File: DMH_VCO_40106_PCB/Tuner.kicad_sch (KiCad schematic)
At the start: 20 parts, among them J11 AVR-ISP-6, SW3 SW_SPDT, U5 ATtiny84A-P, U6 SM420561N

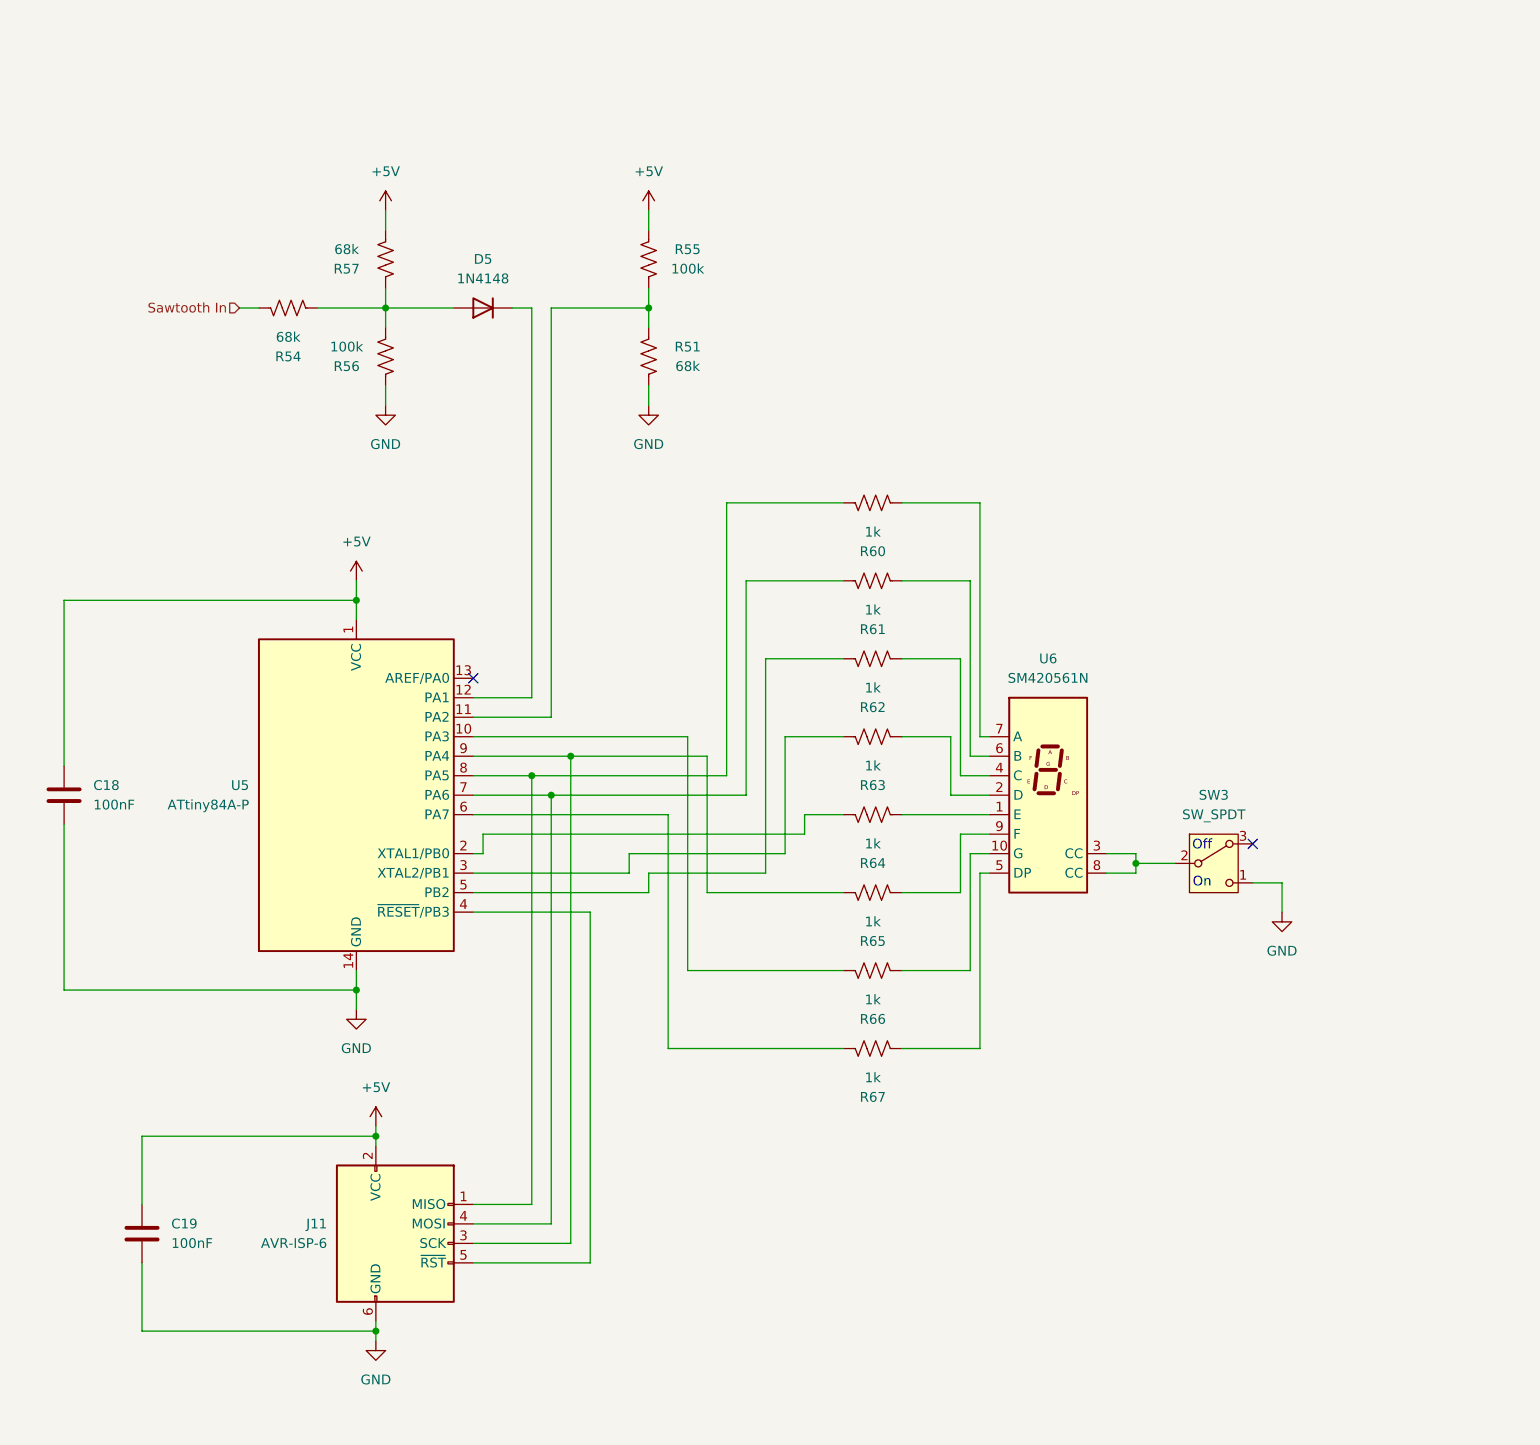
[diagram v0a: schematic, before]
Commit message: Updated Tuner
- Changed uC to ATtiny4313
- Added LEDs
- Created "function" field and updated all jacks, switches and pots
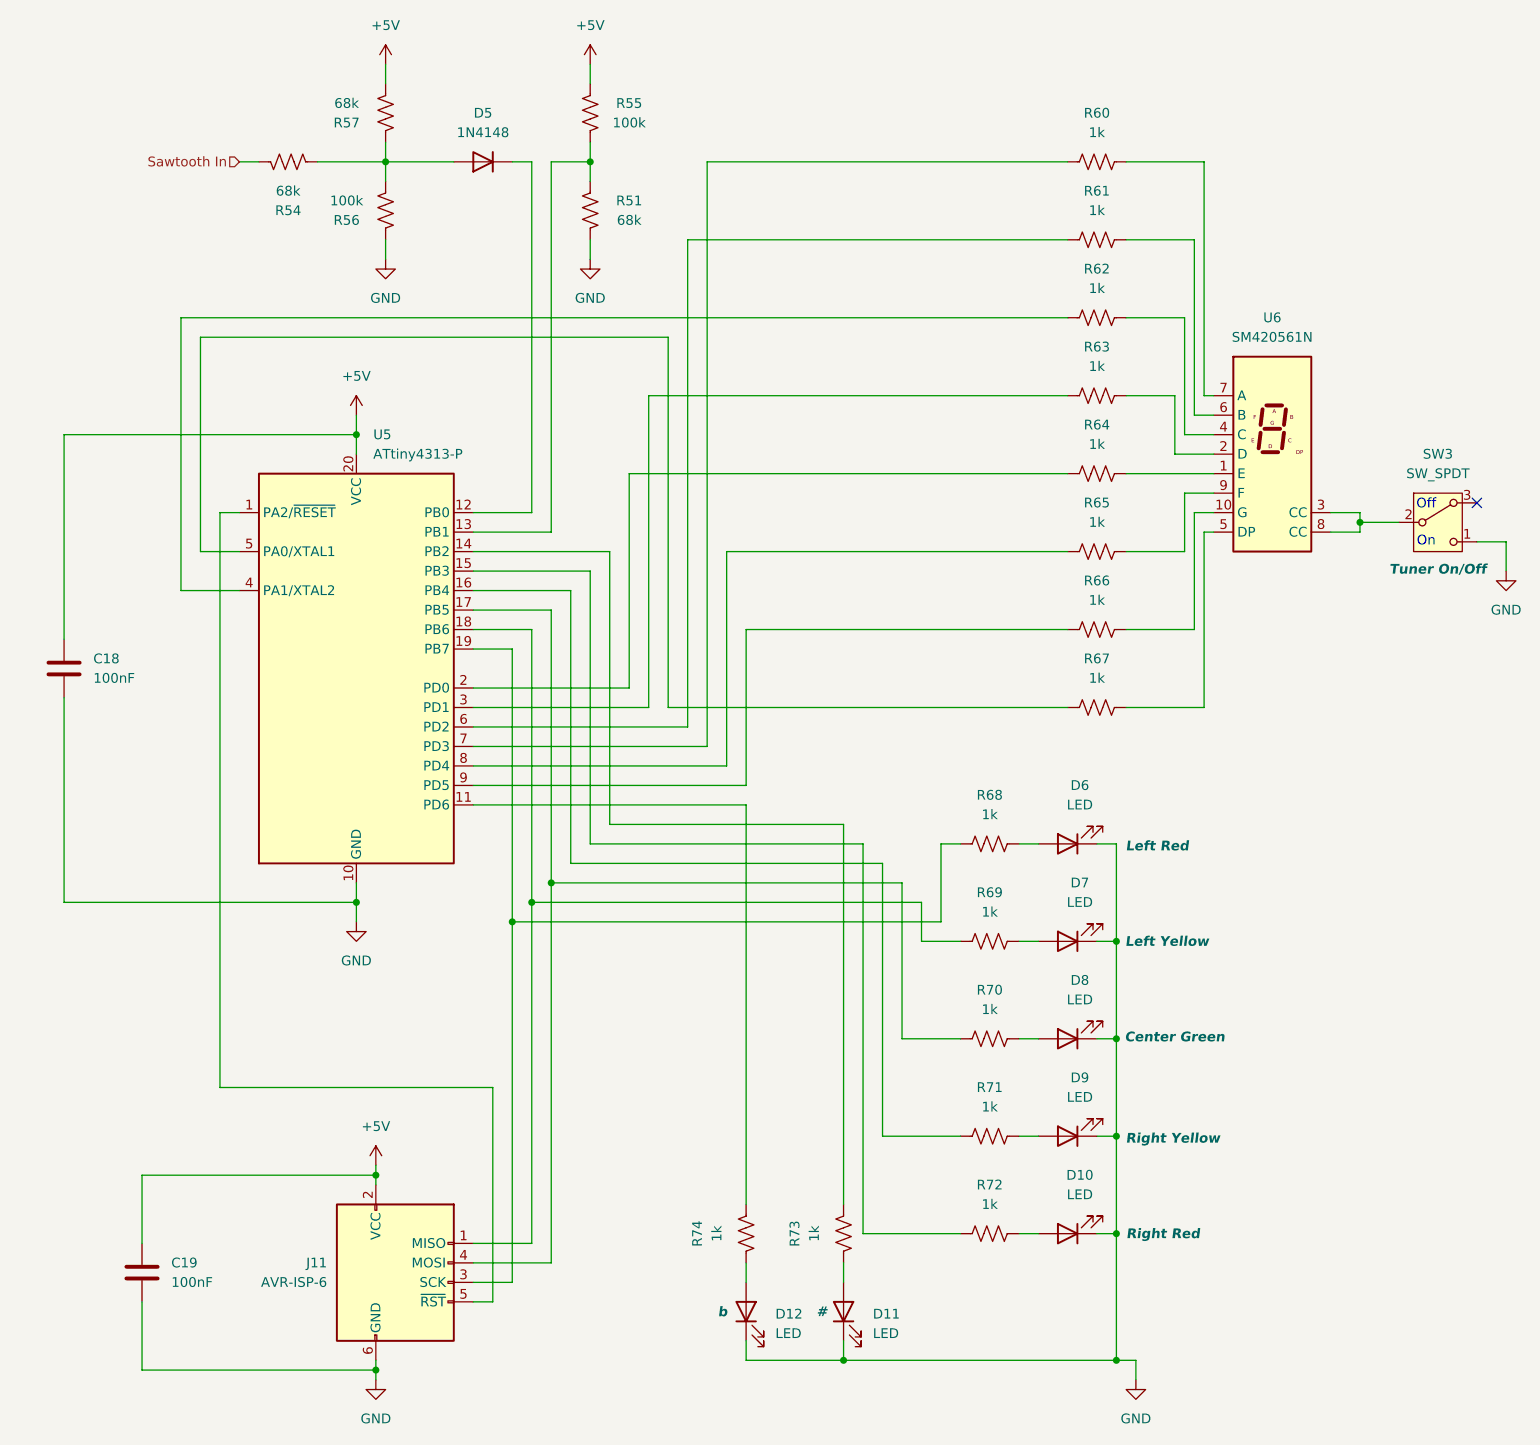
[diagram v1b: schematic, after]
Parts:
- added D10, D11, D12, D6, D7, D8, D9: LED, symbol Device:LED
- added R68, R69, R70, R71, R72, R73, R74: 1k, Resistor_THT:R_Axial_DIN0204_L3.6mm_D1.6mm_P5.08mm_Horizontal, symbol Device:R_US
- SW3: Function (none) -> Tuner On/Off
- U5: value ATtiny84A-P -> ATtiny4313-P; footprint Package_DIP:DIP-14_W7.62mm -> Package_DIP:DIP-20_W7.62mm; symbol MCU_Microchip_ATtiny:ATtiny84A-P -> MCU_Microchip_ATtiny:ATtiny4313-P
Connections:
- net +5V: now also U5.20 (VCC); no longer U5.1 (VCC)
- net GND: now also U5.10 (GND), D10.1 (K), D11.1 (K), D12.1 (K), D6.1 (K), D7.1 (K), D8.1 (K), D9.1 (K); no longer U5.14 (GND)
- net at R66.1: now also U5.9 (PD5); no longer U5.10 (PA3)
- net at R51.2, R55.1: now also U5.13 (PB1); no longer U5.11 (PA2)
- net at J11.5 (~{RST}): now also U5.1 (PA2/~{RESET}); no longer U5.4 (~{RESET}/PB3)
- net at R62.1: now also U5.4 (PA1/XTAL2); no longer U5.5 (PB2)
- net at R67.1: now also U5.5 (PA0/XTAL1); no longer U5.6 (PA7)
- new net: J11.3 (SCK), R68.1, U5.19 (PB7)
- new net: D6.2 (A), R68.2
- new net: R60.1, U5.7 (PD3)
- new net: D12.2 (A), R74.2
- new net: R71.1, U5.16 (PB4)
- new net: D9.2 (A), R71.2
- new net: J11.4 (MOSI), R70.1, U5.17 (PB5)
- new net: D8.2 (A), R70.2
- new net: R74.1, U5.11 (PD6)
- new net: R73.1, U5.14 (PB2)
- new net: R72.1, U5.15 (PB3)
- new net: J11.1 (MISO), R69.1, U5.18 (PB6)
- new net: R61.1, U5.6 (PD2)
- new net: R65.1, U5.8 (PD4)
- new net: D10.2 (A), R72.2
- new net: D11.2 (A), R73.2
- new net: D7.2 (A), R69.2
- no-connect marks 2 -> 1
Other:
- moved on the sheet: C18, C19, D5, J11, R51, R54, R55, R56, R57, R60, R61, R62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

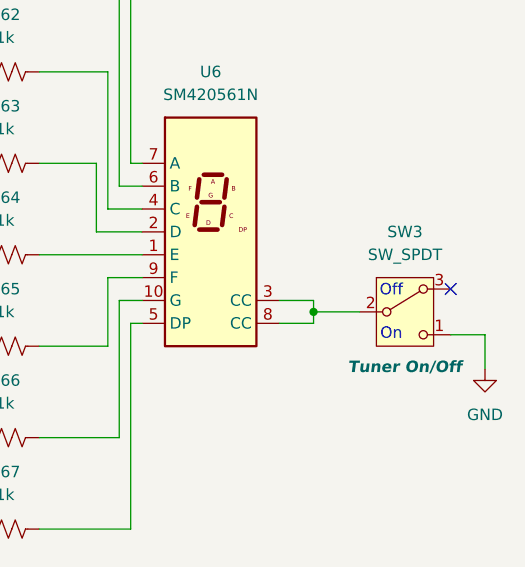
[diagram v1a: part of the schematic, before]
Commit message: Prepared Inputs/Outputs sheet to split in 2 PCBs
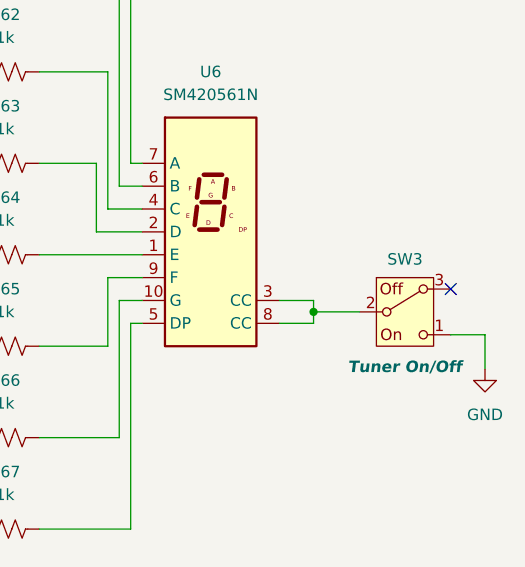
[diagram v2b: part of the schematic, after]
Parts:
- SW3: value SW_SPDT -> SW_SPDT_321_OnOff; symbol Switch:SW_SPDT_321 -> SynthStuff:SW_SPDT_321_OnOff
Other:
- note removed: "Off"
- note removed: "On"
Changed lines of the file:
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@@
-		)
-	)
-	(text "Off"
-		(exclude_from_sim no)
-		(at 202.946 76.454 0)
-		(effects
-			(font
-				(size 1.27 1.27)
-			)
-		)
-	)
-	(text "On"
-		(exclude_from_sim no)
-		(at 202.946 81.28 0)
-		(effects
-			(font
-				(size 1.27 1.27)
-			)
 		)
 	)
@@
 	)
 	(symbol
-		(lib_id "Switch:SW_SPDT_321")
+		(lib_id "SynthStuff:SW_SPDT_321_OnOff")
 		(at 204.47 78.74 0)
 		(unit 1)
@@
 		(dnp no)
 		(property "Reference" "SW3"
-			(at 204.47 69.85 0)
-			(effects
-				(font
-					(size 1.27 1.27)
-				)
-			)
-		)
-		(property "Value" "SW_SPDT"
-			(at 204.47 72.39 0)
-			(effects
-				(font
-					(size 1.27 1.27)
-				)
-			)
-		)
+			(at 204.47 72.898 0)
+			(effects
+				(font
+					(size 1.27 1.27)
+				)
+			)
+		)
+		(property "Value" "SW_SPDT_321_OnOff"
+			(at 204.47 83.82 0)
+			(effects
+				(font
+					(size 1.27 1.27)
+				)
+				(hide yes)
+			)
+		)

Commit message: Started positioning components on PCB
Moving some input resistores from main PCB to Jacks PCB
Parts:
- D10, D11, D12, D6, D7, D8, D9: footprint (none) -> LED_THT:LED_D3.0mm
- R51, R54, R55, R56, R57, R60, R61, R62, R63, R64, R65, R66, R67, R68, R69, R70, R71, R72, R73, R74: footprint Resistor_THT:R_Axial_DIN0204_L3.6mm_D1.6mm_P5.08mm_Horizontal -> Resistor_THT:R_Axial_DIN0207_L6.3mm_D2.5mm_P7.62mm_Horizontal
- SW3: footprint (none) -> SynthStuff:Toggle_Switch_THT
- U5: footprint Package_DIP:DIP-20_W7.62mm -> Package_DIP:DIP-20_W7.62mm_Socket
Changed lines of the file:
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@@
 			)
 		)
-		(property "Footprint" "Resistor_THT:R_Axial_DIN0204_L3.6mm_D1.6mm_P5.08mm_Horizontal"
+		(property "Footprint" "Resistor_THT:R_Axial_DIN0207_L6.3mm_D2.5mm_P7.62mm_Horizontal"
 			(at 146.304 119.634 90)
 			(effects
@@
 			)
 		)
-		(property "Footprint" "Resistor_THT:R_Axial_DIN0204_L3.6mm_D1.6mm_P5.08mm_Horizontal"
+		(property "Footprint" "Resistor_THT:R_Axial_DIN0207_L6.3mm_D2.5mm_P7.62mm_Horizontal"
 			(at 160.274 91.694 90)
 			(effects
@@
 			)
 		)
-		(property "Footprint" "Resistor_THT:R_Axial_DIN0204_L3.6mm_D1.6mm_P5.08mm_Horizontal"
+		(property "Footprint" "Resistor_THT:R_Axial_DIN0207_L6.3mm_D2.5mm_P7.62mm_Horizontal"
 			(at 160.274 30.734 90)
 			(effects
@@
 			)
 		)
-		(property "Footprint" ""
+		(property "Footprint" "LED_THT:LED_D3.0mm"
 			(at 114.3 181.61 0)
 			(effects
@@
 			)
 		)
-		(property "Footprint" "Resistor_THT:R_Axial_DIN0204_L3.6mm_D1.6mm_P5.08mm_Horizontal"
+		(property "Footprint" "Resistor_THT:R_Axial_DIN0207_L6.3mm_D2.5mm_P7.62mm_Horizontal"
 			(at 146.304 157.734 90)
 			(effects
@@
 			)
 		)
-		(property "Footprint" "Resistor_THT:R_Axial_DIN0204_L3.6mm_D1.6mm_P5.08mm_Horizontal"
+		(property "Footprint" "Resistor_THT:R_Axial_DIN0207_L6.3mm_D2.5mm_P7.62mm_Horizontal"
 			(at 146.304 145.034 90)
 			(effects
@@
 			)
 		)
-		(property "Footprint" "Resistor_THT:R_Axial_DIN0204_L3.6mm_D1.6mm_P5.08mm_Horizontal"
+		(property "Footprint" "Resistor_THT:R_Axial_DIN0207_L6.3mm_D2.5mm_P7.62mm_Horizontal"
 			(at 66.294 25.654 90)
 			(effects
@@
 			)
 		)
-		(property "Footprint" "Package_DIP:DIP-20_W7.62mm"
+		(property "Footprint" "Package_DIP:DIP-20_W7.62mm_Socket"
 			(at 63.5 97.79 0)
 			(effects
@@
 			)
 		)
-		(property "Footprint" "Resistor_THT:R_Axial_DIN0204_L3.6mm_D1.6mm_P5.08mm_Horizontal"
+		(property "Footprint" "Resistor_THT:R_Axial_DIN0207_L6.3mm_D2.5mm_P7.62mm_Horizontal"
 			(at 160.274 40.894 90)
 			(effects
@@
 			)
 		)
-		(property "Footprint" "Resistor_THT:R_Axial_DIN0204_L3.6mm_D1.6mm_P5.08mm_Horizontal"
+		(property "Footprint" "Resistor_THT:R_Axial_DIN0207_L6.3mm_D2.5mm_P7.62mm_Horizontal"
 			(at 160.274 61.214 90)
 			(effects
@@
 			)
 		)
-		(property "Footprint" "Resistor_THT:R_Axial_DIN0204_L3.6mm_D1.6mm_P5.08mm_Horizontal"
+		(property "Footprint" "Resistor_THT:R_Axial_DIN0207_L6.3mm_D2.5mm_P7.62mm_Horizontal"
 			(at 94.996 37.846 90)
 			(effects
@@
 			)
 		)
-		(property "Footprint" ""
+		(property "Footprint" "LED_THT:LED_D3.0mm"
 			(at 156.21 171.45 0)
 			(effects
@@
 			)
 		)
-		(property "Footprint" "Resistor_THT:R_Axial_DIN0204_L3.6mm_D1.6mm_P5.08mm_Horizontal"
+		(property "Footprint" "Resistor_THT:R_Axial_DIN0207_L6.3mm_D2.5mm_P7.62mm_Horizontal"
 			(at 160.274 101.854 90)
 			(effects
@@
 			)
 		)
-		(property "Footprint" "Resistor_THT:R_Axial_DIN0204_L3.6mm_D1.6mm_P5.08mm_Horizontal"
+		(property "Footprint" "Resistor_THT:R_Axial_DIN0207_L6.3mm_D2.5mm_P7.62mm_Horizontal"
 			(at 160.274 81.534 90)
 			(effects
@@
 			)
 		)
-		(property "Footprint" "Resistor_THT:R_Axial_DIN0204_L3.6mm_D1.6mm_P5.08mm_Horizontal"
+		(property "Footprint" "Resistor_THT:R_Axial_DIN0207_L6.3mm_D2.5mm_P7.62mm_Horizontal"
 			(at 66.294 38.354 90)
 			(effects
@@
 			)
 		)
-		(property "Footprint" ""
+		(property "Footprint" "LED_THT:LED_D3.0mm"
 			(at 127 181.61 0)
 			(effects
@@
 			)
 		)
-		(property "Footprint" ""
+		(property "Footprint" "LED_THT:LED_D3.0mm"
 			(at 156.21 120.65 0)
 			(effects
@@
 			)
 		)
-		(property "Footprint" "Resistor_THT:R_Axial_DIN0204_L3.6mm_D1.6mm_P5.08mm_Horizontal"
+		(property "Footprint" "Resistor_THT:R_Axial_DIN0207_L6.3mm_D2.5mm_P7.62mm_Horizontal"
 			(at 146.304 132.334 90)
 			(effects
@@
 			)
 		)
-		(property "Footprint" "Resistor_THT:R_Axial_DIN0204_L3.6mm_D1.6mm_P5.08mm_Horizontal"
+		(property "Footprint" "Resistor_THT:R_Axial_DIN0207_L6.3mm_D2.5mm_P7.62mm_Horizontal"
 			(at 113.284 171.704 90)
 			(effects
@@
 			)
 		)
-		(property "Footprint" ""
+		(property "Footprint" "SynthStuff:Toggle_Switch_THT"
 			(at 204.47 88.9 0)
 			(effects
@@
 			)
 		)
-		(property "Footprint" "Resistor_THT:R_Axial_DIN0204_L3.6mm_D1.6mm_P5.08mm_Horizontal"
+		(property "Footprint" "Resistor_THT:R_Axial_DIN0207_L6.3mm_D2.5mm_P7.62mm_Horizontal"
 			(at 146.304 170.434 90)
 			(effects
@@
 			)
 		)
-		(property "Footprint" "Resistor_THT:R_Axial_DIN0204_L3.6mm_D1.6mm_P5.08mm_Horizontal"
+		(property "Footprint" "Resistor_THT:R_Axial_DIN0207_L6.3mm_D2.5mm_P7.62mm_Horizontal"
 			(at 160.274 51.054 90)
 			(effects
@@
 			)
 		)
-		(property "Footprint" "Resistor_THT:R_Axial_DIN0204_L3.6mm_D1.6mm_P5.08mm_Horizontal"
+		(property "Footprint" "Resistor_THT:R_Axial_DIN0207_L6.3mm_D2.5mm_P7.62mm_Horizontal"
 			(at 54.864 32.766 90)
 			(effects
@@
 			)
 		)
-		(property "Footprint" "Resistor_THT:R_Axial_DIN0204_L3.6mm_D1.6mm_P5.08mm_Horizontal"
+		(property "Footprint" "Resistor_THT:R_Axial_DIN0207_L6.3mm_D2.5mm_P7.62mm_Horizontal"
 			(at 160.274 71.374 90)
 			(effects
@@
 			)
 		)
-		(property "Footprint" ""
+		(property "Footprint" "LED_THT:LED_D3.0mm"
 			(at 156.21 158.75 0)
 			(effects
@@
 			)
 		)
-		(property "Footprint" ""
+		(property "Footprint" "LED_THT:LED_D3.0mm"
 			(at 156.21 133.35 0)
 			(effects
@@
 			)
 		)
-		(property "Footprint" "Resistor_THT:R_Axial_DIN0204_L3.6mm_D1.6mm_P5.08mm_Horizontal"
+		(property "Footprint" "Resistor_THT:R_Axial_DIN0207_L6.3mm_D2.5mm_P7.62mm_Horizontal"
 			(at 94.996 25.146 90)
 			(effects
@@
 			)
 		)
-		(property "Footprint" ""
+		(property "Footprint" "LED_THT:LED_D3.0mm"
 			(at 156.21 146.05 0)
 			(effects
@@
 			)
 		)
-		(property "Footprint" "Resistor_THT:R_Axial_DIN0204_L3.6mm_D1.6mm_P5.08mm_Horizontal"
+		(property "Footprint" "Resistor_THT:R_Axial_DIN0207_L6.3mm_D2.5mm_P7.62mm_Horizontal"
 			(at 125.984 171.704 90)
 			(effects
